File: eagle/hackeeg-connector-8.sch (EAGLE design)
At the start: 13 parts

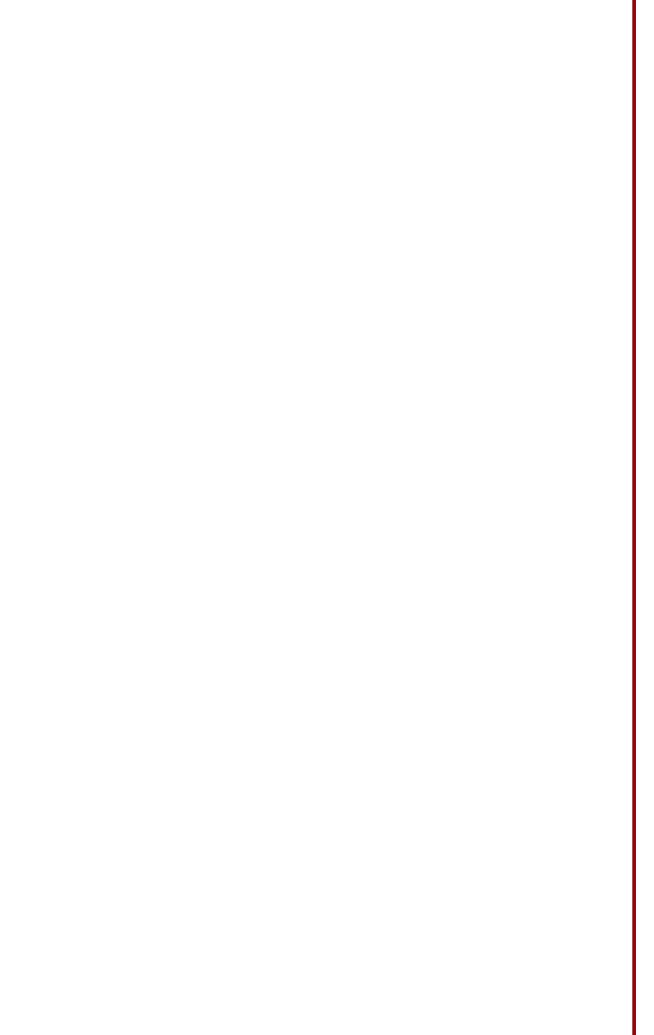
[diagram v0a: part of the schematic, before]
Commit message: made board smaller; trace width increased to 12mil
- from 8mil
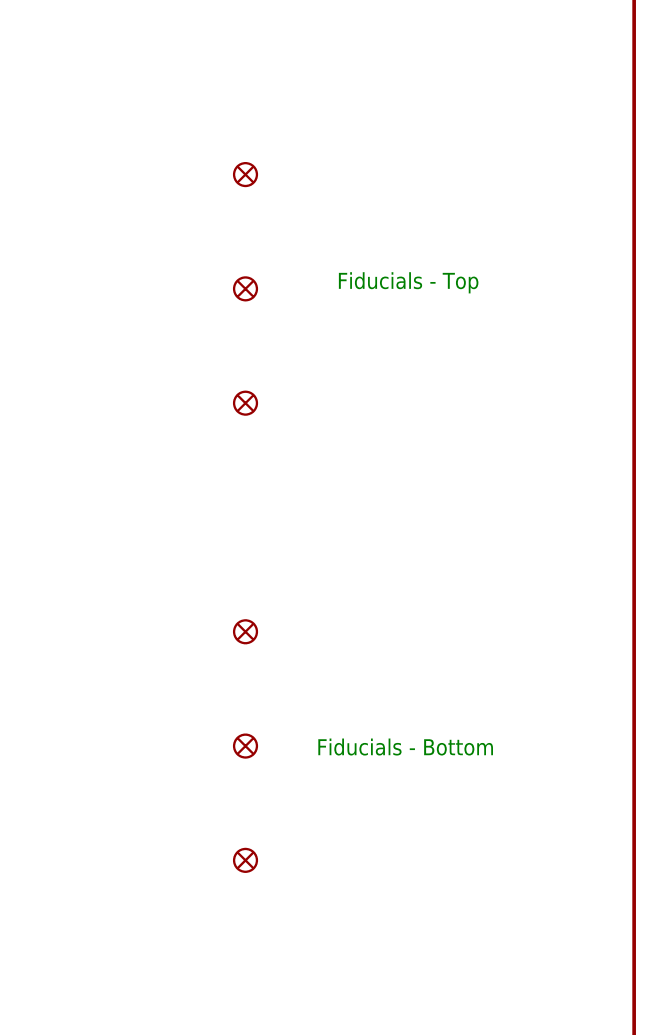
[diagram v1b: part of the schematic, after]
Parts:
- added FD1, FD2, FD3, FD4, FD5, FD6: FIDUCIAL1X2, SparkFun-Aesthetics:FIDUCIAL1X2
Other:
- note added: "Fiducials - Bottom"
- note added: "Fiducials - Top"
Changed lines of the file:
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@@
 <part name="IN8P" library="po-37729" deviceset="PO37729" device="HEX-100"/>
 <part name="U$1" library="endless-knot" deviceset="ENDLESSKNOT" device="ENDLESSKNOT-MEDIUM"/>
+<part name="FD1" library="SparkFun-Aesthetics" library_urn="urn:adsk.eagle:library:507" deviceset="FIDUCIAL" device="1X2" package3d_urn="urn:adsk.eagle:package:37108/1"/>
+<part name="FD2" library="SparkFun-Aesthetics" library_urn="urn:adsk.eagle:library:507" deviceset="FIDUCIAL" device="1X2" package3d_urn="urn:adsk.eagle:package:37108/1"/>
+<part name="FD3" library="SparkFun-Aesthetics" library_urn="urn:adsk.eagle:library:507" deviceset="FIDUCIAL" device="1X2" package3d_urn="urn:adsk.eagle:package:37108/1"/>
+<part name="FD4" library="SparkFun-Aesthetics" library_urn="urn:adsk.eagle:library:507" deviceset="FIDUCIAL" device="1X2" package3d_urn="urn:adsk.eagle:package:37108/1"/>
+<part name="FD5" library="SparkFun-Aesthetics" library_urn="urn:adsk.eagle:library:507" deviceset="FIDUCIAL" device="1X2" package3d_urn="urn:adsk.eagle:package:37108/1"/>
+<part name="FD6" library="SparkFun-Aesthetics" library_urn="urn:adsk.eagle:library:507" deviceset="FIDUCIAL" device="1X2" package3d_urn="urn:adsk.eagle:package:37108/1"/>
 </parts>
 <sheets>
 <sheet>
-<description>HACKEEG Connector Test Board</description>
+<description>HACKEEG 8 Position Connector  Board</description>
 <plain>
+<text x="365.76" y="182.88" size="1.778" layer="91">Fiducials - Top</text>
+<text x="363.474" y="131.064" size="1.778" layer="91">Fiducials - Bottom</text>
 </plain>
 <instances>
@@
 <instance part="IN8P" gate="G$1" x="238.506" y="109.982" rot="MR0"/>
 <instance part="U$1" gate="G$1" x="167.64" y="63.5"/>
+<instance part="FD1" gate="G$1" x="355.6" y="170.18"/>
+<instance part="FD2" gate="G$1" x="355.6" y="182.88"/>
+<instance part="FD3" gate="G$1" x="355.6" y="195.58"/>
+<instance part="FD4" gate="G$1" x="355.6" y="144.78"/>
+<instance part="FD5" gate="G$1" x="355.6" y="132.08"/>
+<instance part="FD6" gate="G$1" x="355.6" y="119.38"/>
 </instances>
 <busses>

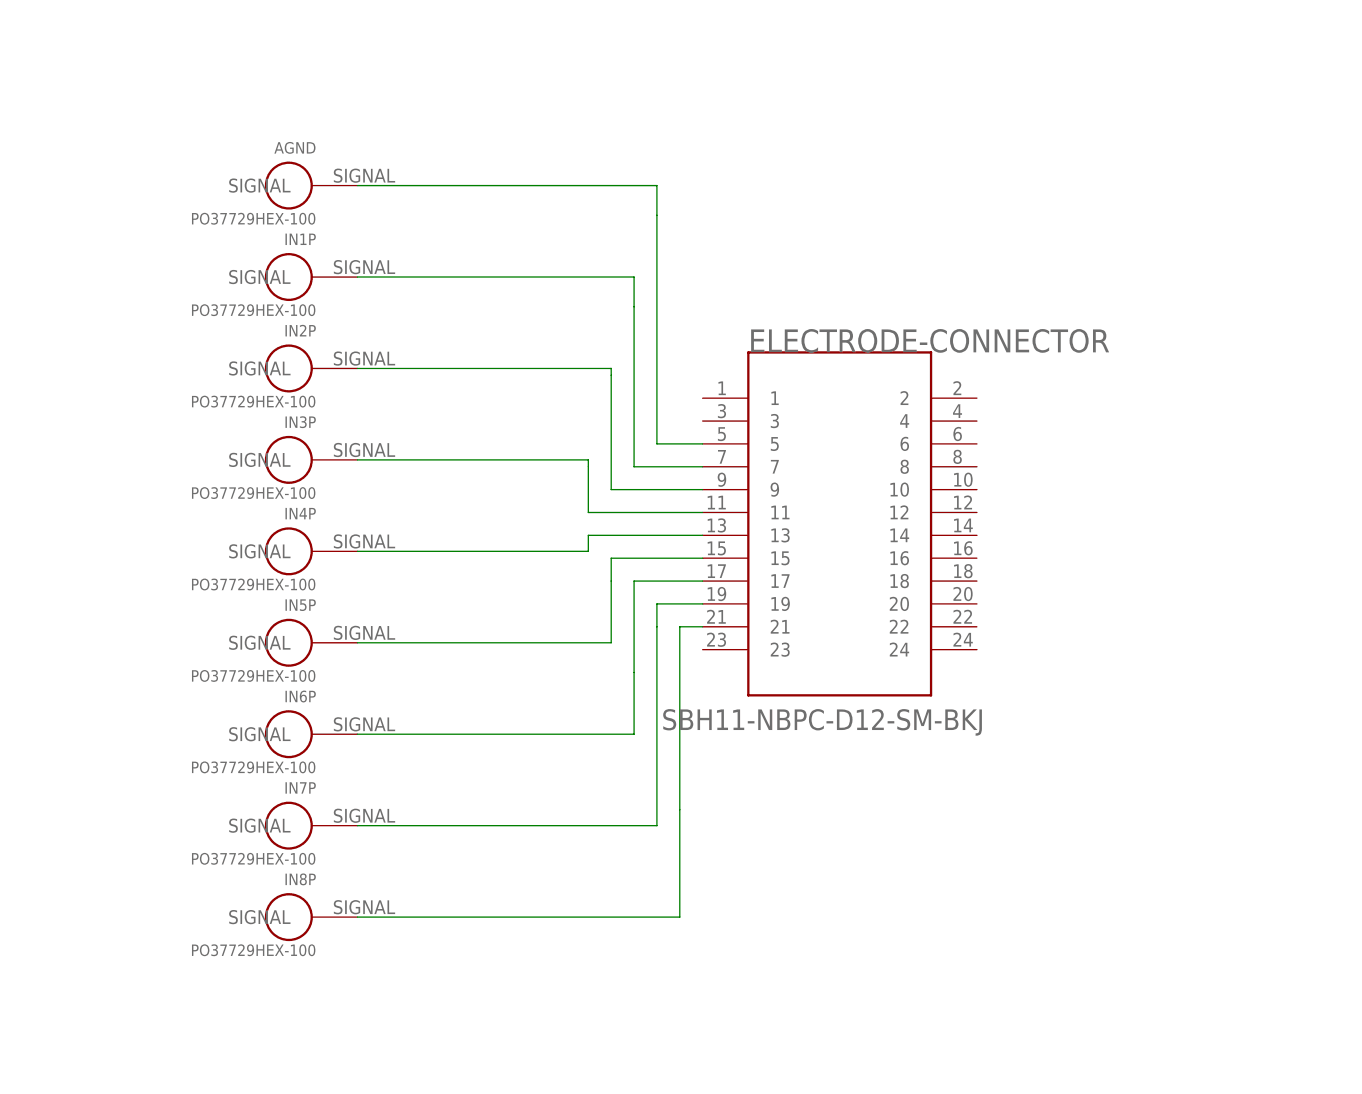
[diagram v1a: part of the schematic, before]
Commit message: updated libraries, rerouted board
- used new SnapEDA footprint for electrode connector
- updated po-37729 to hex110 package
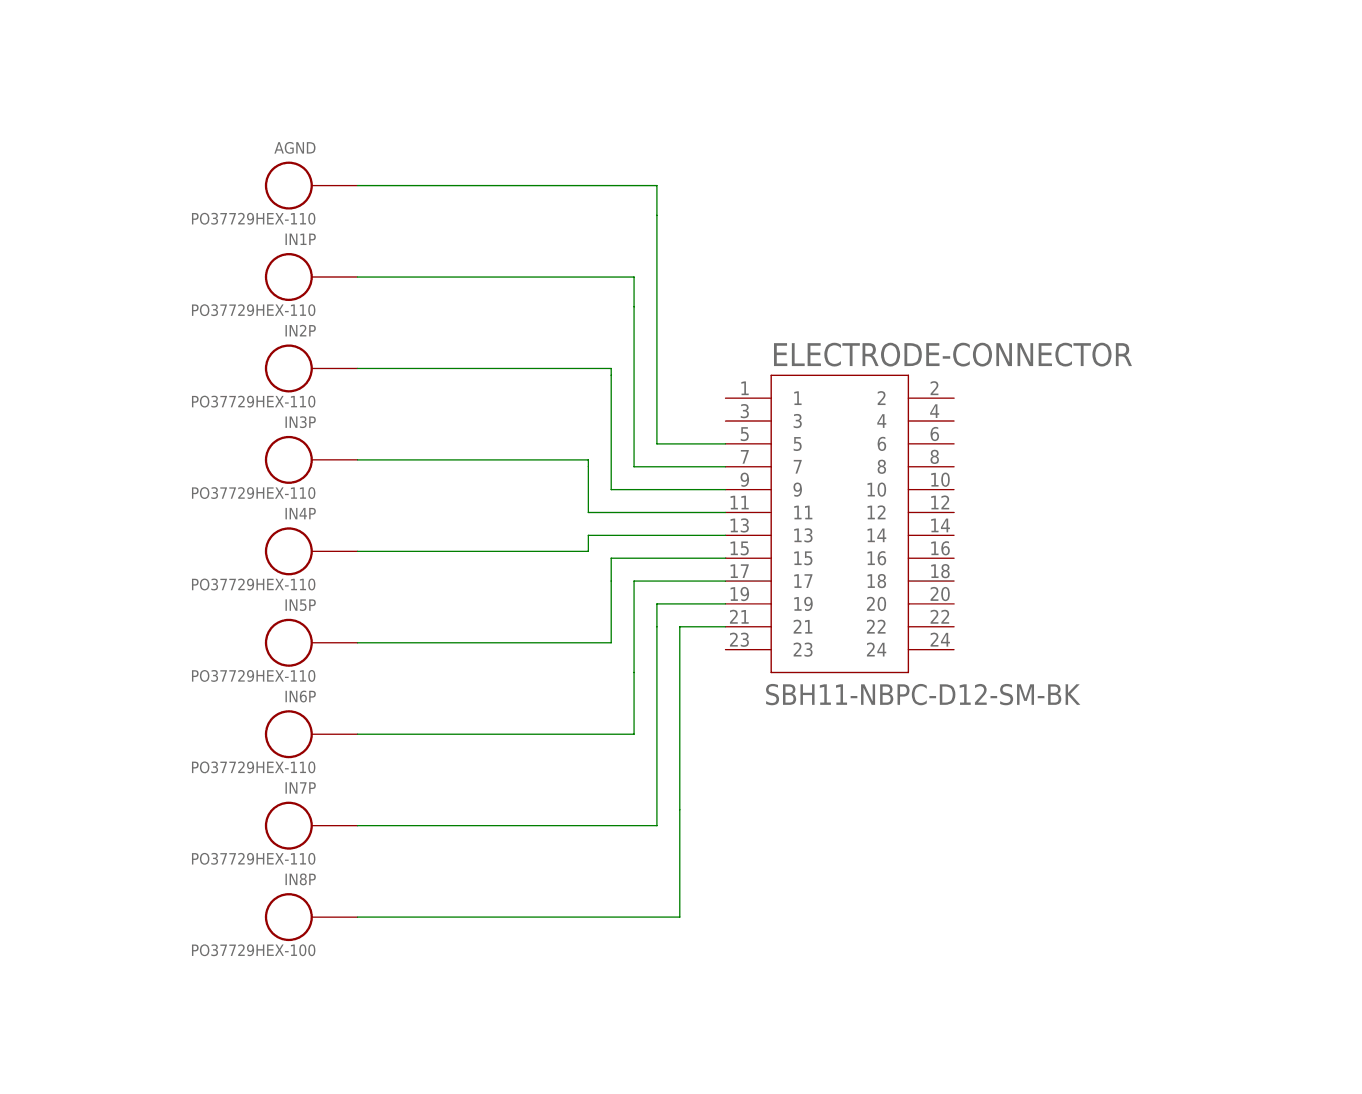
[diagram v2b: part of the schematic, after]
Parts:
- AGND, IN1P, IN2P, IN3P, IN4P, IN5P, IN6P, IN7P: value PO37729HEX-100 -> PO37729HEX-110; device po-37729:PO37729HEX-100 -> po-37729:PO37729HEX-110
- ELECTRODE-CONNECTOR: value SBH11-NBPC-D12-SM-BKJ -> SBH11-NBPC-D12-SM-BK; device SBH11-NBPC-D12-SM-BK:SBH11-NBPC-D12-SM-BKJ -> SBH11-NBPC-D12-SM-BK:SBH11-NBPC-D12-SM-BK

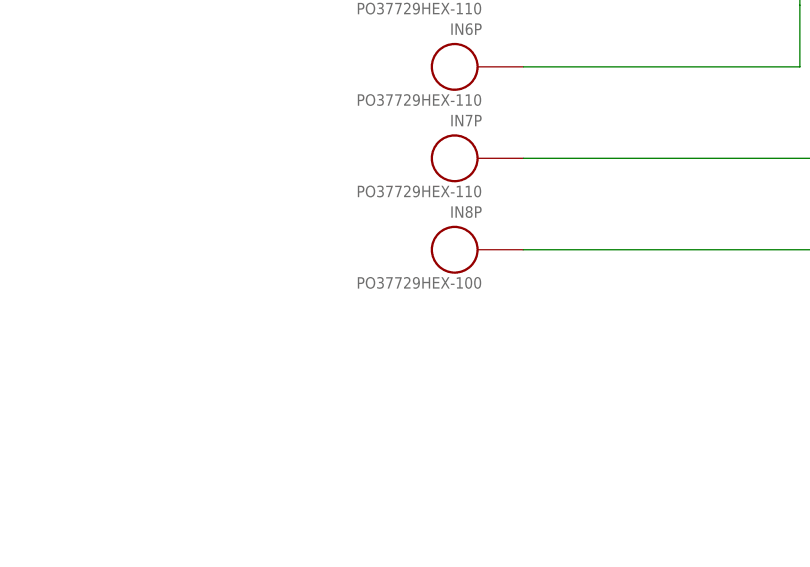
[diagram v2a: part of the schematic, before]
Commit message: removed all po-37729 variants
- since hex110 (110%) is working fine
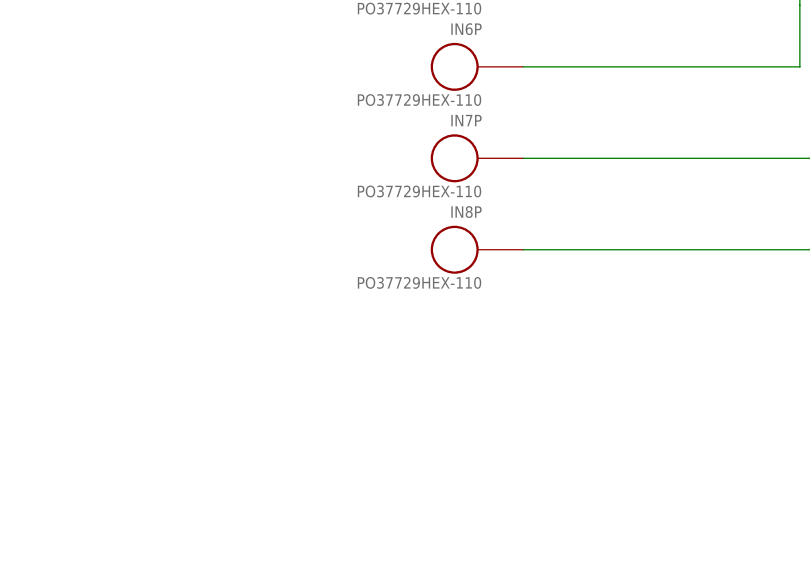
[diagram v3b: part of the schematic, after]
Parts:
- IN8P: value PO37729HEX-100 -> PO37729HEX-110; device po-37729:PO37729HEX-100 -> po-37729:PO37729HEX-110
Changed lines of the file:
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@@
 <grid distance="0.1" unitdist="inch" unit="inch" style="lines" multiple="1" display="no" altdistance="0.01" altunitdist="inch" altunit="inch"/>
 <layers>
-<layer number="1" name="Top" color="4" fill="1" visible="yes" active="no"/>
-<layer number="2" name="Route2" color="16" fill="1" visible="yes" active="no"/>
-<layer number="3" name="Route3" color="17" fill="1" visible="yes" active="no"/>
-<layer number="4" name="Route4" color="18" fill="1" visible="yes" active="no"/>
-<layer number="5" name="Route5" color="19" fill="1" visible="yes" active="no"/>
-<layer number="6" name="Route6" color="25" fill="1" visible="yes" active="no"/>
-<layer number="7" name="Route7" color="26" fill="1" visible="yes" active="no"/>
-<layer number="8" name="Route8" color="27" fill="1" visible="yes" active="no"/>
-<layer number="9" name="Route9" color="28" fill="1" visible="yes" active="no"/>
-<layer number="10" name="Route10" color="29" fill="1" visible="yes" active="no"/>
-<layer number="11" name="Route11" color="30" fill="1" visible="yes" active="no"/>
-<layer number="12" name="Route12" color="20" fill="1" visible="yes" active="no"/>
-<layer number="13" name="Route13" color="21" fill="1" visible="yes" active="no"/>
-<layer number="14" name="Route14" color="22" fill="1" visible="yes" active="no"/>
-<layer number="15" name="Route15" color="23" fill="1" visible="yes" active="no"/>
-<layer number="16" name="Bottom" color="1" fill="1" visible="yes" active="no"/>
-<layer number="17" name="Pads" color="2" fill="1" visible="yes" active="no"/>
-<layer number="18" name="Vias" color="2" fill="1" visible="yes" active="no"/>
-<layer number="19" name="Unrouted" color="6" fill="1" visible="yes" active="no"/>
-<layer number="20" name="Dimension" color="24" fill="1" visible="yes" active="no"/>
-<layer number="21" name="tPlace" color="7" fill="1" visible="yes" active="no"/>
-<layer number="22" name="bPlace" color="7" fill="1" visible="yes" active="no"/>
-<layer number="23" name="tOrigins" color="15" fill="1" visible="yes" active="no"/>
-<layer number="24" name="bOrigins" color="15" fill="1" visible="yes" active="no"/>
-<layer number="25" name="tNames" color="7" fill="1" visible="yes" active="no"/>
-<layer number="26" name="bNames" color="7" fill="1" visible="yes" active="no"/>
-<layer number="27" name="tValues" color="7" fill="1" visible="yes" active="no"/>
-<layer number="28" name="bValues" color="7" fill="1" visible="yes" active="no"/>
+<layer number="1" name="Top" color="4" fill="1" visible="no" active="no"/>
+<layer number="2" name="Route2" color="16" fill="1" visible="no" active="no"/>
+<layer number="3" name="Route3" color="17" fill="1" visible="no" active="no"/>
+<layer number="4" name="Route4" color="18" fill="1" visible="no" active="no"/>
+<layer number="5" name="Route5" color="19" fill="1" visible="no" active="no"/>
+<layer number="6" name="Route6" color="25" fill="1" visible="no" active="no"/>
+<layer number="7" name="Route7" color="26" fill="1" visible="no" active="no"/>
+<layer number="8" name="Route8" color="27" fill="1" visible="no" active="no"/>
+<layer number="9" name="Route9" color="28" fill="1" visible="no" active="no"/>
+<layer number="10" name="Route10" color="29" fill="1" visible="no" active="no"/>
+<layer number="11" name="Route11" color="30" fill="1" visible="no" active="no"/>
+<layer number="12" name="Route12" color="20" fill="1" visible="no" active="no"/>
+<layer number="13" name="Route13" color="21" fill="1" visible="no" active="no"/>
+<layer number="14" name="Route14" color="22" fill="1" visible="no" active="no"/>
+<layer number="15" name="Route15" color="23" fill="1" visible="no" active="no"/>
+<layer number="16" name="Bottom" color="1" fill="1" visible="no" active="no"/>
+<layer number="17" name="Pads" color="2" fill="1" visible="no" active="no"/>
+<layer number="18" name="Vias" color="2" fill="1" visible="no" active="no"/>
+<layer number="19" name="Unrouted" color="6" fill="1" visible="no" active="no"/>
+<layer number="20" name="Dimension" color="24" fill="1" visible="no" active="no"/>
+<layer number="21" name="tPlace" color="7" fill="1" visible="no" active="no"/>
+<layer number="22" name="bPlace" color="7" fill="1" visible="no" active="no"/>
+<layer number="23" name="tOrigins" color="15" fill="1" visible="no" active="no"/>
+<layer number="24" name="bOrigins" color="15" fill="1" visible="no" active="no"/>
+<layer number="25" name="tNames" color="7" fill="1" visible="no" active="no"/>
+<layer number="26" name="bNames" color="7" fill="1" visible="no" active="no"/>
+<layer number="27" name="tValues" color="7" fill="1" visible="no" active="no"/>
+<layer number="28" name="bValues" color="7" fill="1" visible="no" active="no"/>
 <layer number="29" name="tStop" color="7" fill="3" visible="no" active="no"/>
 <layer number="30" name="bStop" color="7" fill="6" visible="no" active="no"/>
@@
 <layer number="35" name="tGlue" color="7" fill="4" visible="no" active="no"/>
 <layer number="36" name="bGlue" color="7" fill="5" visible="no" active="no"/>
-<layer number="37" name="tTest" color="7" fill="1" visible="yes" active="no"/>
-<layer number="38" name="bTest" color="7" fill="1" visible="yes" active="no"/>
+<layer number="37" name="tTest" color="7" fill="1" visible="no" active="no"/>
+<layer number="38" name="bTest" color="7" fill="1" visible="no" active="no"/>
 <layer number="39" name="tKeepout" color="4" fill="11" visible="no" active="no"/>
 <layer number="40" name="bKeepout" color="1" fill="11" visible="no" active="no"/>
@@
 <layer number="44" name="Drills" color="7" fill="1" visible="no" active="no"/>
 <layer number="45" name="Holes" color="7" fill="1" visible="no" active="no"/>
-<layer number="46" name="Milling" color="3" fill="1" visible="yes" active="no"/>
-<layer number="47" name="Measures" color="7" fill="1" visible="yes" active="no"/>
-<layer number="48" name="Document" color="7" fill="1" visible="yes" active="no"/>
-<layer number="49" name="Reference" color="7" fill="1" visible="yes" active="no"/>
-<layer number="50" name="dxf" color="7" fill="1" visible="yes" active="no"/>
-<layer number="51" name="tDocu" color="7" fill="1" visible="yes" active="no"/>
-<layer number="52" name="bDocu" color="7" fill="1" visible="yes" active="no"/>
-<layer number="53" name="tGND_GNDA" color="7" fill="9" visible="yes" active="no"/>
-<layer number="54" name="bGND_GNDA" color="1" fill="9" visible="yes" active="no"/>
-<layer number="56" name="wert" color="7" fill="1" visible="yes" active="no"/>
-<layer number="57" name="tCAD" color="7" fill="1" visible="yes" active="no"/>
-<layer number="59" name="tCarbon" color="7" fill="1" visible="yes" active="no"/>
-<layer number="60" name="bCarbon" color="7" fill="1" visible="yes" active="no"/>
+<layer number="46" name="Milling" color="3" fill="1" visible="no" active="no"/>
+<layer number="47" name="Measures" color="7" fill="1" visible="no" active="no"/>
+<layer number="48" name="Document" color="7" fill="1" visible="no" active="no"/>
+<layer number="49" name="Reference" color="7" fill="1" visible="no" active="no"/>
+<layer number="50" name="dxf" color="7" fill="1" visible="no" active="no"/>
+<layer number="51" name="tDocu" color="7" fill="1" visible="no" active="no"/>
+<layer number="52" name="bDocu" color="7" fill="1" visible="no" active="no"/>
+<layer number="53" name="tGND_GNDA" color="7" fill="9" visible="no" active="no"/>
+<layer number="54" name="bGND_GNDA" color="1" fill="9" visible="no" active="no"/>
+<layer number="56" name="wert" color="7" fill="1" visible="no" active="no"/>
+<layer number="57" name="tCAD" color="7" fill="1" visible="no" active="no"/>
+<layer number="59" name="tCarbon" color="7" fill="1" visible="no" active="no"/>
+<layer number="60" name="bCarbon" color="7" fill="1" visible="no" active="no"/>
 <layer number="88" name="SimResults" color="9" fill="1" visible="yes" active="yes"/>
 <layer number="89" name="SimProbes" color="9" fill="1" visible="yes" active="yes"/>
@@
 <part name="IN7P" library="po-37729" deviceset="PO37729" device="HEX-110" value="PO37729HEX-110"/>
 <part name="AGND" library="po-37729" deviceset="PO37729" device="HEX-110" value="PO37729HEX-110"/>
-<part name="IN8P" library="po-37729" deviceset="PO37729" device="HEX-100"/>
+<part name="IN8P" library="po-37729" deviceset="PO37729" device="HEX-110"/>
 <part name="U$1" library="endless-knot" deviceset="ENDLESSKNOT" device="ENDLESSKNOT-MEDIUM"/>
 <part name="FD1" library="SparkFun-Aesthetics" library_urn="urn:adsk.eagle:library:507" deviceset="FIDUCIAL" device="1X2" package3d_urn="urn:adsk.eagle:package:37108/1"/>
